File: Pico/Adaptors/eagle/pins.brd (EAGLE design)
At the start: 26 x 20.6 mm, 4 parts

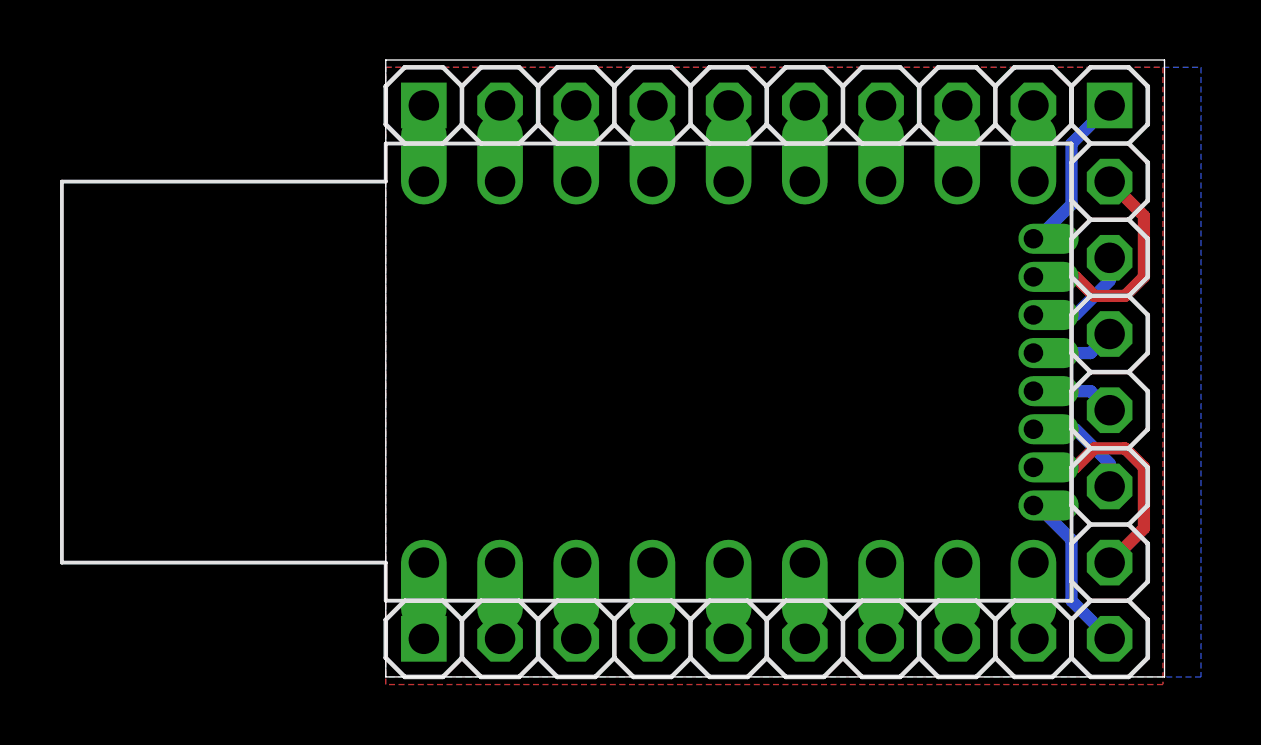
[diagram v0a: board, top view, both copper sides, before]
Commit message: add JST connector to pins, update thumbnails
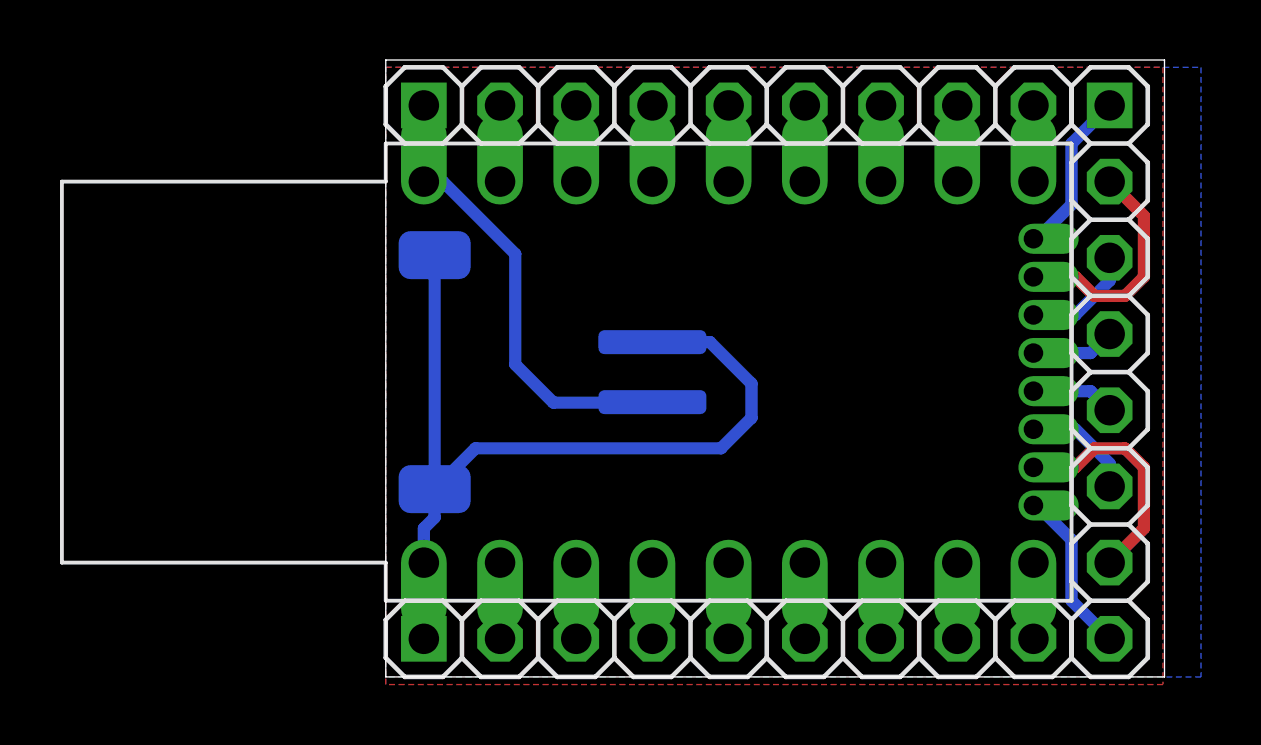
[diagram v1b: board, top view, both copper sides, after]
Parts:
- added J1: JST-2P-SMD-PW-3410050P1, OPL Eagle Library:2P-SMD-2.0-90D
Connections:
- removed net N$15: JP3.1, U$1.BAT
- new net BAT: J1.+, JP3.1, U$1.BAT
- net GND: now also J1.-, J1.3, J1.4
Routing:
- net GND: track 2.54 -> 29.5 mm
- net BAT: track 0.00 -> 15.4 mm
- net N$15: track 2.54 -> 0.00 mm
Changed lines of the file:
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@@
 <layers>
 <layer number="1" name="Top" color="4" fill="1" visible="yes" active="yes"/>
+<layer number="2" name="Route2" color="1" fill="3" visible="no" active="no"/>
+<layer number="15" name="Route15" color="4" fill="6" visible="no" active="no"/>
 <layer number="16" name="Bottom" color="1" fill="1" visible="yes" active="yes"/>
 <layer number="17" name="Pads" color="2" fill="1" visible="yes" active="yes"/>
@@
 <layer number="48" name="Document" color="7" fill="1" visible="yes" active="yes"/>
 <layer number="49" name="Reference" color="7" fill="1" visible="yes" active="yes"/>
+<layer number="50" name="dxf" color="7" fill="1" visible="yes" active="yes"/>
 <layer number="51" name="tDocu" color="7" fill="1" visible="yes" active="yes"/>
 <layer number="52" name="bDocu" color="7" fill="1" visible="yes" active="yes"/>
+<layer number="53" name="tGND_GNDA" color="7" fill="9" visible="no" active="no"/>
+<layer number="54" name="bGND_GNDA" color="1" fill="9" visible="no" active="no"/>
+<layer number="56" name="wert" color="7" fill="1" visible="no" active="no"/>
 <layer number="91" name="Nets" color="2" fill="1" visible="no" active="no"/>
 <layer number="92" name="Busses" color="1" fill="1" visible="no" active="no"/>
@@
 <layer number="97" name="Info" color="7" fill="1" visible="no" active="no"/>
 <layer number="98" name="Guide" color="6" fill="1" visible="no" active="no"/>
+<layer number="100" name="Muster" color="7" fill="1" visible="no" active="no"/>
+<layer number="101" name="Patch_Top" color="12" fill="4" visible="no" active="no"/>
+<layer number="102" name="Vscore" color="7" fill="1" visible="no" active="no"/>
+<layer number="103" name="tMap" color="7" fill="1" visible="no" active="no"/>
+<layer number="104" name="Name" color="7" fill="1" visible="no" active="no"/>
+<layer number="105" name="tPlate" color="7" fill="1" visible="no" active="no"/>
+<layer number="106" name="bPlate" color="7" fill="1" visible="no" active="no"/>
+<layer number="107" name="Crop" color="7" fill="1" visible="no" active="no"/>
+<layer number="108" name="fp8" color="7" fill="1" visible="no" active="no"/>
+<layer number="109" name="fp9" color="7" fill="1" visible="no" active="no"/>
+<layer number="110" name="110" color="7" fill="1" visible="no" active="no"/>
+<layer number="111" name="111" color="7" fill="1" visible="no" active="no"/>
+<layer number="112" name="tSilk" color="7" fill="1" visible="no" active="no"/>
+<layer number="116" name="Patch_BOT" color="9" fill="4" visible="no" active="no"/>
+<layer number="118" name="Rect_Pads" color="7" fill="1" visible="no" active="no"/>
+<layer number="121" name="_tsilk" color="7" fill="1" visible="no" active="no"/>
+<layer number="122" name="_bsilk" color="7" fill="1" visible="no" active="no"/>
+<layer number="123" name="tTestmark" color="7" fill="1" visible="no" active="no"/>
+<layer number="124" name="bTestmark" color="7" fill="1" visible="no" active="no"/>
+<layer number="125" name="_tNames" color="7" fill="1" visible="no" active="no"/>
+<layer number="126" name="_bNames" color="7" fill="1" visible="no" active="no"/>
+<layer number="127" name="_tValues" color="7" fill="1" visible="no" active="no"/>
+<layer number="128" name="_bValues" color="7" fill="1" visible="no" active="no"/>
+<layer number="131" name="tAdjust" color="7" fill="1" visible="no" active="no"/>
+<layer number="132" name="bAdjust" color="7" fill="1" visible="no" active="no"/>
+<layer number="144" name="DrillLegend" color="7" fill="1" visible="no" active="no"/>
+<layer number="151" name="HeatSink" color="14" fill="1" visible="no" active="no"/>
+<layer number="152" name="_bDocu" color="7" fill="1" visible="no" active="no"/>
+<layer number="199" name="Contour" color="7" fill="1" visible="no" active="no"/>
+<layer number="200" name="200bmp" color="1" fill="10" visible="no" active="no"/>
+<layer number="201" name="201bmp" color="2" fill="1" visible="no" active="no"/>
+<layer number="202" name="202bmp" color="3" fill="1" visible="no" active="no"/>
+<layer number="203" name="203bmp" color="4" fill="10" visible="no" active="no"/>
+<layer number="204" name="204bmp" color="5" fill="10" visible="no" active="no"/>
+<layer number="205" name="205bmp" color="6" fill="10" visible="no" active="no"/>
+<layer number="206" name="206bmp" color="7" fill="10" visible="no" active="no"/>
+<layer number="207" name="207bmp" color="15" fill="10" visible="no" active="no"/>
+<layer number="208" name="208bmp" color="9" fill="10" visible="no" active="no"/>
+<layer number="209" name="209bmp" color="7" fill="1" visible="no" active="no"/>
+<layer number="210" name="210bmp" color="7" fill="1" visible="no" active="no"/>
+<layer number="211" name="211bmp" color="7" fill="1" visible="no" active="no"/>
+<layer number="212" name="212bmp" color="7" fill="1" visible="no" active="no"/>
+<layer number="213" name="213bmp" color="7" fill="1" visible="no" active="no"/>
+<layer number="214" name="214bmp" color="7" fill="1" visible="no" active="no"/>
+<layer number="215" name="215bmp" color="7" fill="1" visible="no" active="no"/>
+<layer number="216" name="216bmp" color="7" fill="1" visible="no" active="no"/>
+<layer number="217" name="217bmp" color="18" fill="1" visible="no" active="no"/>
+<layer number="218" name="218bmp" color="19" fill="1" visible="no" active="no"/>
+<layer number="219" name="219bmp" color="20" fill="1" visible="no" active="no"/>
+<layer number="220" name="220bmp" color="21" fill="1" visible="no" active="no"/>
+<layer number="221" name="221bmp" color="22" fill="1" visible="no" active="no"/>
+<layer number="222" name="222bmp" color="23" fill="1" visible="no" active="no"/>
+<layer number="223" name="223bmp" color="24" fill="1" visible="no" active="no"/>
+<layer number="224" name="224bmp" color="25" fill="1" visible="no" active="no"/>
+<layer number="248" name="Housing" color="7" fill="1" visible="no" active="no"/>
+<layer number="249" name="Edge" color="7" fill="1" visible="no" active="no"/>
+<layer number="250" name="Descript" color="3" fill="1" visible="no" active="no"/>
+<layer number="251" name="SMDround" color="12" fill="11" visible="no" active="no"/>
+<layer number="254" name="OrgLBR" color="13" fill="1" visible="no" active="no"/>
 </layers>
 <board>
@@
 <attribute name="VALUE" x="0" y="-1.905" size="1.27" layer="27"/>
 </element>
+<element name="J1" library="OPL Eagle Library" package="2P-SMD-2.0-90D" value="JST-2P-SMD-PW-3410050P1" x="3.81" y="10.16" rot="MR90"/>
 </elements>
 <signals>
@@
 <vertex x="0" y="0"/>
 </polygon>
+<contactref element="J1" pad="-"/>
+<contactref element="J1" pad="3"/>
+<contactref element="J1" pad="4"/>
+<wire x1="8.89" y1="11.16" x2="10.811" y2="11.16" width="0.4064" layer="16"/>
+<wire x1="10.811" y1="11.16" x2="12.192" y2="9.779" width="0.4064" layer="16"/>
+<wire x1="12.192" y1="9.779" x2="12.192" y2="8.636" width="0.4064" layer="16"/>
+<wire x1="12.192" y1="8.636" x2="11.176" y2="7.62" width="0.4064" layer="16"/>
+<wire x1="11.176" y1="7.62" x2="2.989" y2="7.62" width="0.4064" layer="16"/>
+<wire x1="2.989" y1="7.62" x2="1.629" y2="6.26" width="0.4064" layer="16"/>
+<wire x1="1.629" y1="6.26" x2="1.629" y2="14.06" width="0.4064" layer="16"/>
+<wire x1="1.629" y1="6.26" x2="1.629" y2="5.312" width="0.4064" layer="16"/>
+<wire x1="1.629" y1="5.312" x2="1.27" y2="4.953" width="0.4064" layer="16"/>
+<wire x1="1.27" y1="4.953" x2="1.27" y2="3.81" width="0.4064" layer="16"/>
 </signal>
 <signal name="N$9">
@@
 <wire x1="21.59" y1="3.81" x2="21.59" y2="1.27" width="1.016" layer="16"/>
 </signal>
-<signal name="N$15">
+<signal name="BAT">
 <contactref element="U$1" pad="BAT"/>
 <contactref element="JP3" pad="1"/>
 <wire x1="1.27" y1="16.51" x2="1.27" y2="19.05" width="1.016" layer="16"/>
+<contactref element="J1" pad="+"/>
+<wire x1="1.27" y1="16.51" x2="1.905" y2="16.51" width="0.4064" layer="16"/>
+<wire x1="1.905" y1="16.51" x2="4.318" y2="14.097" width="0.4064" layer="16"/>
+<wire x1="4.318" y1="14.097" x2="4.318" y2="10.414" width="0.4064" layer="16"/>
+<wire x1="4.318" y1="10.414" x2="5.588" y2="9.144" width="0.4064" layer="16"/>
+<wire x1="5.588" y1="9.144" x2="8.874" y2="9.144" width="0.4064" layer="16"/>
+<wire x1="8.874" y1="9.144" x2="8.89" y2="9.16" width="0.4064" layer="16"/>
 </signal>
 <signal name="N$16">
